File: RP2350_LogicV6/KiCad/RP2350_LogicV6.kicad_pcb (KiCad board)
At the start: 4 copper layers, 50 x 50 mm, 69 parts, among them J2 Conn_02x16_Odd_Even, J3 SWD, J4 USB_B_Micro, J5 2350 BOOT SEL, J6 SWD, J7 SWD, J9 VGA, U1 TXU0104PWR, U10 RP2350A-QFN60, U2 TXU0104PWR, U3 TXU0104PWR, U4 TXU0104PWR, U5 TXU0104PWR, U6 TXU0104PWR, U7 LD1117S33TR_SOT223, U8 TLV74311PDBVR, U9 W25Q16JVSSIQ, Y1 12MHz

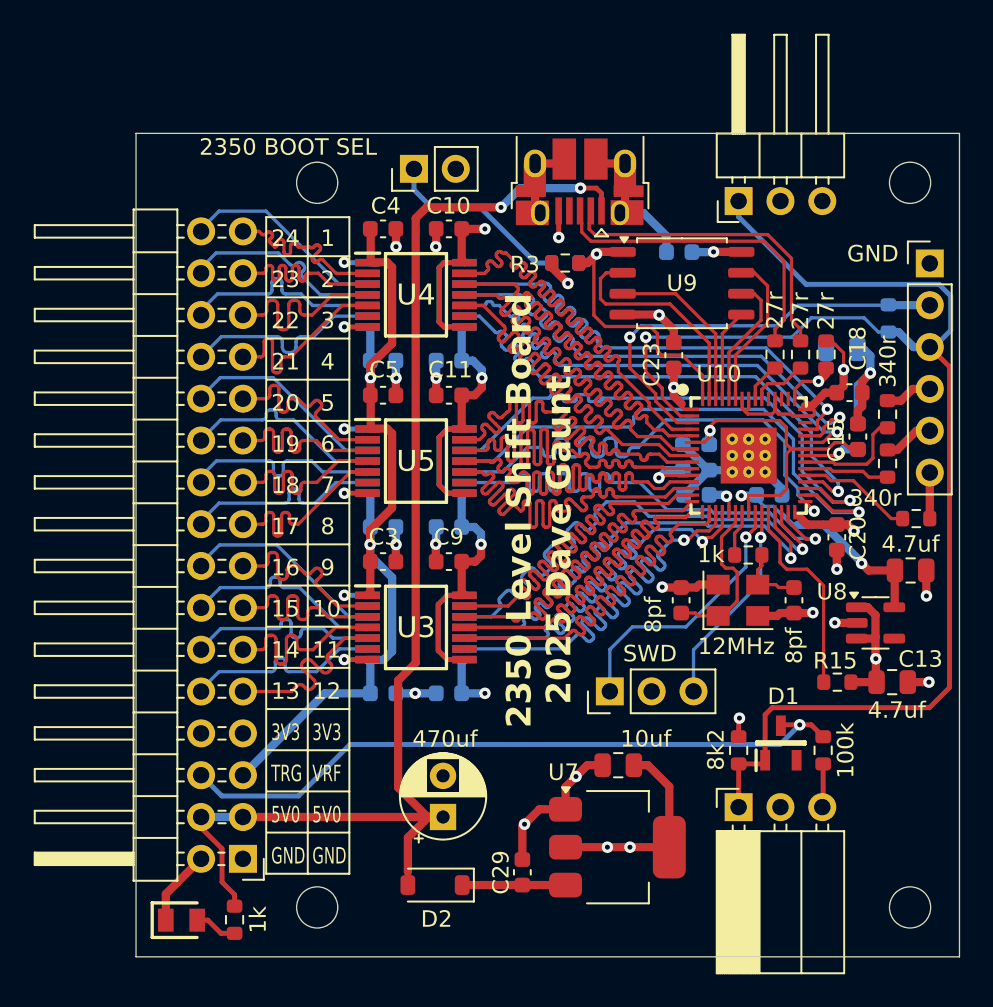
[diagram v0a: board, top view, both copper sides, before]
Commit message: - Updated To KiCad 10
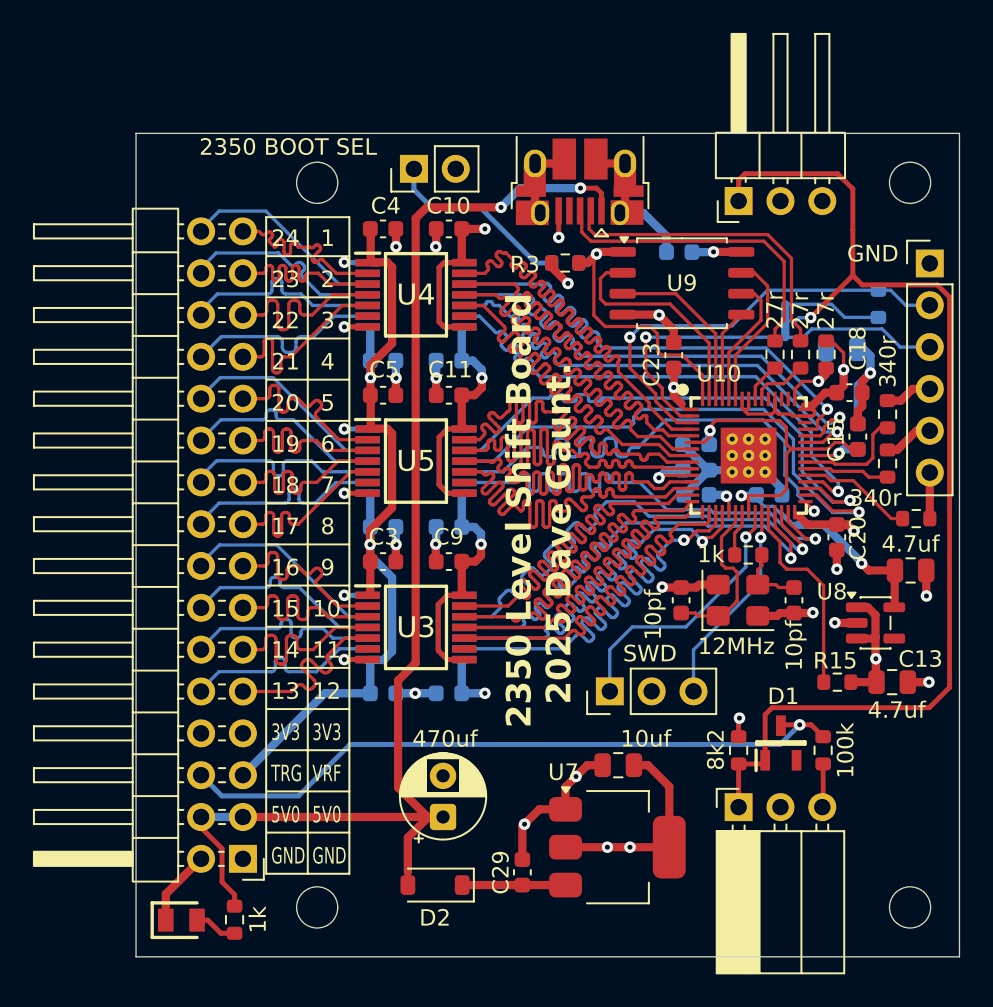
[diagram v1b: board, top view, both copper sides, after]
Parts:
- added NT1: NetTie_3, NetTie:NetTie-3_SMD_Pad0.5mm, B.Cu at (151.4, 96.9)
- C26, C27: value 8pf -> 10pf
- D2: value B140-E3 -> ~
- moved R10 1.07 mm to (157.1, 95.8)
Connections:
- net V_SYNC renamed /V_SYNC
- J9 pad 3: EXT_CHAIN -> /H_SYNC
- R10 pad 2: EXT_CHAIN -> Net-(NT1-Pad3)
- U10 pad 2: EXT_CHAIN -> /H_SYNC
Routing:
- net /H_SYNC: track 0.00 -> 24.3 mm, vias 0 -> 1
- net EXT_CHAIN: track 84.3 -> 68.3 mm
- net Net-(NT1-Pad3): track 0.00 -> 5.98 mm
- net /V_SYNC: track 26.3 -> 27.1 mm
